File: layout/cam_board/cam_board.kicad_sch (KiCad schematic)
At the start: 73 parts, among them J1 Debug, J2 USB Connector, J3 BATT_CONNECTOR, J4 LCD conn, J5 Stick conn, Q1 BSS138, SW1 BOOT0, SW2 NRST, SW3 USER, SW4 ON/OFF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

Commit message: Update layout and schematic
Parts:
- added C6: 100nF, Capacitor_SMD:C_0402_1005Metric_Pad0.74x0.62mm_HandSolder, symbol Device:C
- added R23, R24: 10k, Resistor_SMD:R_0603_1608Metric_Pad0.98x0.95mm_HandSolder, symbol Device:R
- added U3: M24C16-RMN6TP, A_Custom:SOIC127P600X175-8N, symbol Custom:M24C16-RMN6TP
- SW1, SW2, SW4: footprint Button_Switch_SMD:SW_DIP_SPSTx01_Slide_9.78x4.72mm_W8.61mm_P2.54mm -> Button_Switch_SMD:SW_DIP_SPSTx01_Slide_6.7x4.1mm_W8.61mm_P2.54mm_LowProfile
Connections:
- net +3V3: now also C6.2, R23.2, R24.1, U3.8 (VCC)
- net GND: now also C6.1, U3.1 (E0), U3.2 (E1), U3.3 (E2), U3.4 (VSS)
- net EEPROM_NWC: now reaches U1.41 (PB5)
- net EEPROM_NWC: now also U3.7 (~{WC})
- net EEPROM_SCL: now reaches U1.42 (PB6)
- net EEPROM_SCL: now also R23.1, U3.6 (SCL)
- net EEPROM_SDA: now reaches U1.43 (PB7)
- net EEPROM_SDA: now also R24.2, U3.5 (SDA)
- no-connect marks 8 -> 5
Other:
- note added: "I2C-EEPROM"
- note removed: "SPI-Flash?"
- moved on the sheet: C10, C11, C12, C13, C18, C8, C9, R1, R2, R7, SW1, SW2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

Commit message: Update layout and schematic
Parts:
- added JP1: Battery Bypass, Jumper:SolderJumper-3_P1.3mm_Open_RoundedPad1.0x1.5mm_NumberLabels, symbol Jumper:SolderJumper_3_Open
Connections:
- net VIN: now also JP1.2 (C); no longer C21.2, U5.18 (IN), U5.19 (IN)
- net VOUT: now also JP1.1 (A)
- new net: C21.2, JP1.3 (B), U5.18 (IN), U5.19 (IN)
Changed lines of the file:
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@@
 	)
 	(junction
-		(at 220.98 33.02)
-		(diameter 0)
-		(color 0 0 0 0)
-	)
-	(junction
 		(at 137.16 35.56)
 		(diameter 0)
@@
 	)
 	(junction
+		(at 220.98 34.29)
+		(diameter 0)
+		(color 0 0 0 0)
+	)
+	(junction
 		(at 187.96 35.56)
 		(diameter 0)
@@
 	)
 	(junction
-		(at 224.79 29.21)
+		(at 43.18 185.42)
 		(diameter 0)
 		(color 0 0 0 0)
 	)
 	(junction
-		(at 43.18 185.42)
+		(at 190.5 81.28)
 		(diameter 0)
 		(color 0 0 0 0)
 	)
 	(junction
-		(at 190.5 81.28)
+		(at 228.6 29.21)
 		(diameter 0)
 		(color 0 0 0 0)
@@
 	)
 	(junction
+		(at 238.76 34.29)
+		(diameter 0)
+		(color 0 0 0 0)
+	)
+	(junction
 		(at 270.51 59.69)
 		(diameter 0)
@@
 	(wire
 		(pts
-			(xy 238.76 33.02) (xy 238.76 43.18)
+			(xy 238.76 33.02) (xy 238.76 34.29)
 		)
 		(stroke
@@
 	(wire
 		(pts
+			(xy 220.98 34.29) (xy 220.98 35.56)
+		)
+		(stroke
+			(width 0)
+			(type default)
+		)
+	)
+	(wire
+		(pts
 			(xy 43.18 184.15) (xy 43.18 185.42)
 		)
@@
 	(wire
 		(pts
-			(xy 224.79 29.21) (xy 237.49 29.21)
+			(xy 224.79 29.21) (xy 228.6 29.21)
 		)
 		(stroke
@@
 	(wire
 		(pts
-			(xy 220.98 33.02) (xy 220.98 35.56)
+			(xy 220.98 33.02) (xy 220.98 34.29)
 		)
 		(stroke
@@
 	(wire
 		(pts
-			(xy 220.98 33.02) (xy 224.79 33.02)
-		)
-		(stroke
-			(width 0)
-			(type default)
-		)
-	)
-	(wire
-		(pts
 			(xy 209.55 118.11) (xy 209.55 123.19)
 		)
@@
 	(wire
 		(pts
+			(xy 233.68 34.29) (xy 238.76 34.29)
+		)
+		(stroke
+			(width 0)
+			(type default)
+		)
+	)
+	(wire
+		(pts
 			(xy 158.75 45.72) (xy 158.75 44.45)
 		)
@@
 	(wire
 		(pts
+			(xy 238.76 34.29) (xy 238.76 43.18)
+		)
+		(stroke
+			(width 0)
+			(type default)
+		)
+	)
+	(wire
+		(pts
 			(xy 250.19 73.66) (xy 250.19 74.93)
 		)
@@
 	(wire
 		(pts
+			(xy 228.6 29.21) (xy 228.6 30.48)
+		)
+		(stroke
+			(width 0)
+			(type default)
+		)
+	)
+	(wire
+		(pts
 			(xy 43.18 173.99) (xy 43.18 175.26)
 		)
@@
 	(wire
 		(pts
+			(xy 228.6 29.21) (xy 237.49 29.21)
+		)
+		(stroke
+			(width 0)
+			(type default)
+		)
+	)
+	(wire
+		(pts
 			(xy 190.5 81.28) (xy 190.5 83.82)
 		)
@@
 	(wire
 		(pts
+			(xy 220.98 34.29) (xy 223.52 34.29)
+		)
+		(stroke
+			(width 0)
+			(type default)
+		)
+	)
+	(wire
+		(pts
 			(xy 151.13 173.99) (xy 153.67 173.99)
 		)
@@
 	(wire
 		(pts
-			(xy 224.79 29.21) (xy 224.79 33.02)
-		)
-		(stroke
-			(width 0)
-			(type default)
-		)
-	)
-	(wire
-		(pts
 			(xy 218.44 24.13) (xy 213.36 24.13)
 		)
@@
 					(unit 1)
 				)
+			)
+		)
+	)
+	(symbol
+		(lib_id "Jumper:SolderJumper_3_Open")
+		(at 228.6 34.29 180)
+		(unit 1)
+		(exclude_from_sim no)
+		(in_bom no)
+		(on_board yes)
+		(dnp no)
+		(property "Reference" "JP1"
+			(at 230.886 32.004 0)
+			(effects
+				(font
+					(size 1.27 1.27)
+				)
+			)
+		)
+		(property "Value" "Battery Bypass"
+			(at 229.362 36.83 0)
+			(effects
+				(font
+					(size 1.27 1.27)
+				)
+			)
+		)
+		(property "Footprint" "Jumper:SolderJumper-3_P1.3mm_Open_RoundedPad1.0x1.5mm_NumberLabels"
+			(at 228.6 34.29 0)
+			(effects
+				(font
+					(size 1.27 1.27)
+				)
+				(hide yes)
+			)
+		)
+		(property "Datasheet" "~"
+			(at 228.6 34.29 0)
+			(effects
+				(font
+					(size 1.27 1.27)
+				)
+				(hide yes)
+			)
+		)
+		(property "Description" "Solder Jumper, 3-pole, open"
+			(at 228.6 34.29 0)
+			(effects
+				(font
+					(size 1.27 1.27)
+				)
+				(hide yes)
+			)
+		)
+		(pin "3"
+		)
+		(pin "2"
+		)
+		(pin "1"
+		)
+		(instances
+			(project "cam_board"
+				(path "/eee23683-93c4-45fa-9c00-e358d0d25f58"
+					(reference "JP1")
+					(unit 1)
+				)

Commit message: Update layout and schematic
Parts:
- removed D2, D3: D_Schottky, Diode_SMD:D_0603_1608Metric_Pad1.05x0.95mm_HandSolder, symbol Device:D_Schottky
- removed J1: Debug, Connector_PinHeader_1.27mm:PinHeader_1x06_P1.27mm_Vertical, symbol Connector:Conn_01x06_Pin
- removed Q1: BSS138, Package_TO_SOT_SMD:SOT-23_Handsoldering, symbol Transistor_FET:BSS138
- added J1: Conn_01x04_Pin, Connector_PinHeader_1.27mm:PinHeader_1x04_P1.27mm_Vertical, symbol Connector:Conn_01x04_Pin
- C6: footprint Capacitor_SMD:C_0402_1005Metric_Pad0.74x0.62mm_HandSolder -> Capacitor_SMD:C_0603_1608Metric_Pad1.08x0.95mm_HandSolder
- R17: value 100k -> 100M
- R18: value 220k -> 220M
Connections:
- net USB+5V is gone; now on net VIN: C14.2, C15.2, D5.1 (K), U2.5 (VBUS)
- net GND: now also R18.1
- net NRST: now also J1.4 (Pin_4)
- net SWCLK: now also J1.1 (Pin_1)
- net SWDIO: now also J1.2 (Pin_2)
- net SWO: now also J1.3 (Pin_3)
- net BATTLVL_READ: no longer names the net of U1.25 (PB12)
- no-connect marks 5 -> 6
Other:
- note removed: "With the diode-or one can safely connect the LDO both with USB or Debug voltage ToDo: kann der SWD den ladestrom?"
- moved on the sheet: C23, R17, R18

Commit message: Update layout and schematic
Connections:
- net SWCLK: now also U1.37 (PA14); no longer U1.34 (PA13)
- net SWDIO: now also U1.34 (PA13); no longer U1.37 (PA14)
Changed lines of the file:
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@@
 		)
 	)
-	(global_label "SWDIO"
-		(shape input)
-		(at 156.21 95.25 0)
-		(fields_autoplaced yes)
-		(effects
-			(font
-				(size 1.27 1.27)
-			)
-			(justify left)
-		)
-		(property "Intersheetrefs" "${INTERSHEET_REFS}"
-			(at 165.0614 95.25 0)
-			(effects
-				(font
-					(size 1.27 1.27)
-				)
-				(justify left)
-				(hide yes)
-			)
-		)
-	)
 	(global_label "DC"
 		(shape input)
@@
 		)
 	)
+	(global_label "SWDIO"
+		(shape input)
+		(at 156.21 92.71 0)
+		(fields_autoplaced yes)
+		(effects
+			(font
+				(size 1.27 1.27)
+			)
+			(justify left)
+		)
+		(property "Intersheetrefs" "${INTERSHEET_REFS}"
+			(at 165.0614 92.71 0)
+			(effects
+				(font
+					(size 1.27 1.27)
+				)
+				(justify left)
+				(hide yes)
+			)
+		)
+	)
 	(global_label "D+"
 		(shape input)
@@
 		)
 	)
-	(global_label "SWCLK"
-		(shape input)
-		(at 156.21 92.71 0)
-		(fields_autoplaced yes)
-		(effects
-			(font
-				(size 1.27 1.27)
-			)
-			(justify left)
-		)
-		(property "Intersheetrefs" "${INTERSHEET_REFS}"
-			(at 165.4242 92.71 0)
-			(effects
-				(font
-					(size 1.27 1.27)
-				)
-				(justify left)
-				(hide yes)
-			)
-		)
-	)
 	(global_label "BATTCHARGE"
 		(shape input)
@@
 		)
 	)
+	(global_label "SWCLK"
+		(shape input)
+		(at 156.21 95.25 0)
+		(fields_autoplaced yes)
+		(effects
+			(font
+				(size 1.27 1.27)
+			)
+			(justify left)
+		)
+		(property "Intersheetrefs" "${INTERSHEET_REFS}"
+			(at 165.4242 95.25 0)
+			(effects
+				(font
+					(size 1.27 1.27)
+				)
+				(justify left)
+				(hide yes)
+			)
+		)
+	)
 	(global_label "BATTCHARGING"
 		(shape input)
@@
 	)
 	(symbol
+		(lib_name "+5V_3")
 		(lib_id "power:+5V")
 		(at 250.19 54.61 0)
@@
 	)
 	(symbol
+		(lib_name "+5V_2")
 		(lib_id "power:+5V")
 		(at 228.6 21.59 0)
@@
 	)
 	(symbol
+		(lib_name "+5V_1")
 		(lib_id "power:+5V")
 		(at 187.96 26.67 0)
@@
 	)
 	(symbol
+		(lib_name "SolderJumper_3_Open_1")
 		(lib_id "Jumper:SolderJumper_3_Open")
 		(at 228.6 34.29 180)

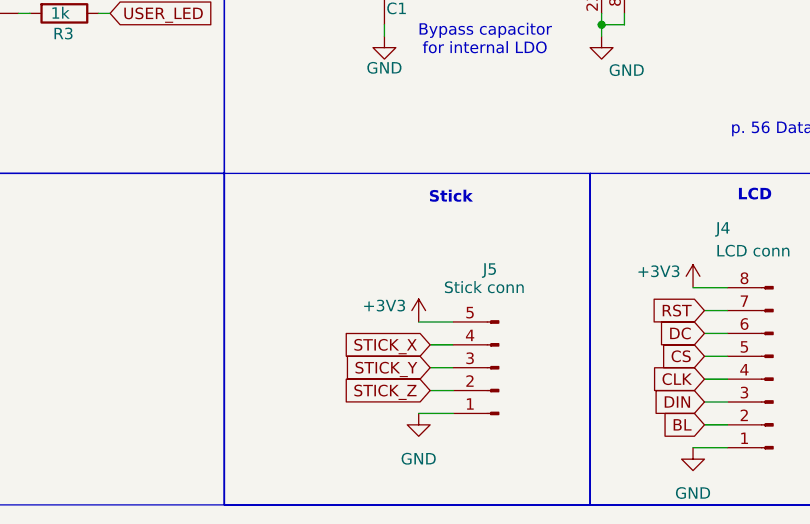
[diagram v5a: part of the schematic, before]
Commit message: Fix menu, add missing pull-up
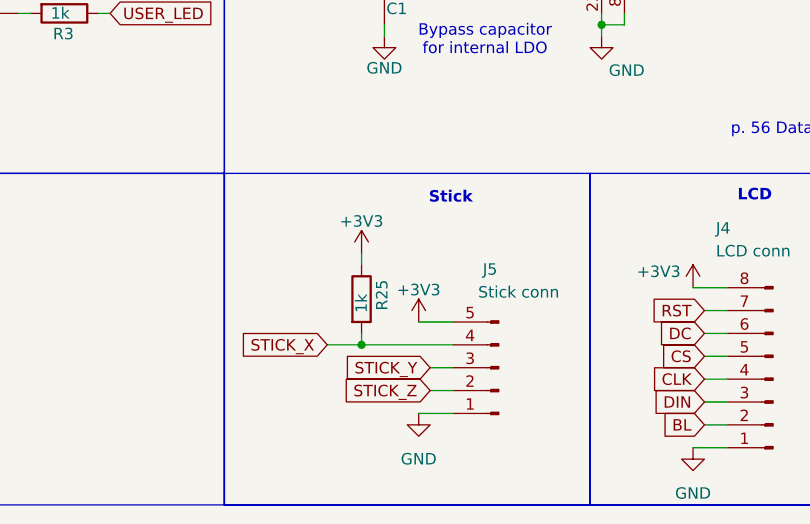
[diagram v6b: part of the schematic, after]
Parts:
- added R25: 1k, Resistor_SMD:R_0603_1608Metric_Pad0.98x0.95mm_HandSolder, symbol Device:R
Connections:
- net +3V3: now also R25.1
- net STICK_X: now also R25.2
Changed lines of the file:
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@@
 	)
 	(junction
+		(at 113.03 177.8)
+		(diameter 0)
+		(color 0 0 0 0)
+	)
+	(junction
 		(at 74.93 30.48)
 		(diameter 0)
@@
 	(wire
 		(pts
-			(xy 120.65 177.8) (xy 123.19 177.8)
+			(xy 109.22 177.8) (xy 113.03 177.8)
 		)
 		(stroke
@@
 	(wire
 		(pts
+			(xy 113.03 176.53) (xy 113.03 177.8)
+		)
+		(stroke
+			(width 0)
+			(type default)
+		)
+	)
+	(wire
+		(pts
 			(xy 220.98 33.02) (xy 220.98 34.29)
 		)
@@
 	(wire
 		(pts
+			(xy 113.03 167.64) (xy 113.03 168.91)
+		)
+		(stroke
+			(width 0)
+			(type default)
+		)
+	)
+	(wire
+		(pts
 			(xy 243.84 74.93) (xy 250.19 74.93)
 		)
@@
 	(wire
 		(pts
+			(xy 113.03 177.8) (xy 123.19 177.8)
+		)
+		(stroke
+			(width 0)
+			(type default)
+		)
+	)
+	(wire
+		(pts
 			(xy 275.59 125.73) (xy 275.59 124.46)
 		)
@@
 	(global_label "STICK_X"
 		(shape input)
-		(at 120.65 177.8 180)
+		(at 109.22 177.8 180)
 		(fields_autoplaced yes)
 		(effects
@@
 		)
 		(property "Intersheetrefs" "${INTERSHEET_REFS}"
-			(at 110.1658 177.8 0)
+			(at 98.7358 177.8 0)
 			(effects
 				(font
@@
 	)
 	(symbol
+		(lib_id "power:+3V3")
+		(at 113.03 167.64 0)
+		(unit 1)
+		(exclude_from_sim no)
+		(in_bom yes)
+		(on_board yes)
+		(dnp no)
+		(property "Reference" "#PWR02"
+			(at 113.03 171.45 0)
+			(effects
+				(font
+					(size 1.27 1.27)
+				)
+				(hide yes)
+			)
+		)
+		(property "Value" "+3V3"
+			(at 113.03 164.084 0)
+			(effects
+				(font
+					(size 1.27 1.27)
+				)
+			)
+		)
+		(property "Footprint" ""
+			(at 113.03 167.64 0)
+			(effects
+				(font
+					(size 1.27 1.27)
+				)
+				(hide yes)
+			)
+		)
+		(property "Datasheet" ""
+			(at 113.03 167.64 0)
+			(effects
+				(font
+					(size 1.27 1.27)
+				)
+				(hide yes)
+			)
+		)
+		(property "Description" "Power symbol creates a global label with name \"+3V3\""
+			(at 113.03 167.64 0)
+			(effects
+				(font
+					(size 1.27 1.27)
+				)
+				(hide yes)
+			)
+		)
+		(pin "1"
+		)
+		(instances
+			(project "cam_board"
+				(path "/eee23683-93c4-45fa-9c00-e358d0d25f58"
+					(reference "#PWR02")
+					(unit 1)
+				)
+			)
+		)
+	)
+	(symbol
 		(lib_id "power:GND")
 		(at 259.08 125.73 0)
@@
 		)
 		(property "Value" "Stick conn"
-			(at 122.174 171.45 0)
+			(at 125.984 171.958 0)
 			(effects
 				(font
@@
 	)
 	(symbol
+		(lib_id "Device:R")
+		(at 113.03 172.72 0)
+		(unit 1)
+		(exclude_from_sim no)
+		(in_bom yes)
+		(on_board yes)
+		(dnp no)
+		(property "Reference" "R25"
+			(at 115.316 173.99 90)
+			(effects
+				(font
+					(size 1.27 1.27)
+				)
+				(justify left)
+			)
+		)
+		(property "Value" "1k"
+			(at 113.03 174.244 90)
+			(effects
+				(font
+					(size 1.27 1.27)
+				)
+				(justify left)
+			)
+		)
+		(property "Footprint" "Resistor_SMD:R_0603_1608Metric_Pad0.98x0.95mm_HandSolder"
+			(at 111.252 172.72 90)
+			(effects
+				(font
+					(size 1.27 1.27)
+				)
+				(hide yes)
+			)
+		)
+		(property "Datasheet" "~"
+			(at 113.03 172.72 0)
+			(effects
+				(font
+					(size 1.27 1.27)
+				)
+				(hide yes)
+			)
+		)
+		(property "Description" "Resistor"
+			(at 113.03 172.72 0)
+			(effects
+				(font
+					(size 1.27 1.27)
+				)
+				(hide yes)
+			)
+		)
+		(pin "2"
+		)
+		(pin "1"
+		)
+		(instances
+			(project "cam_board"
+				(path "/eee23683-93c4-45fa-9c00-e358d0d25f58"
+					(reference "R25")
+					(unit 1)
+				)
+			)
+		)
+	)
+	(symbol
 		(lib_id "Device:C")
 		(at 109.22 74.93 180)
@@
 		)
 		(property "Value" "+3V3"
-			(at 115.57 173.482 0)
+			(at 119.38 171.704 0)
 			(effects
 				(font

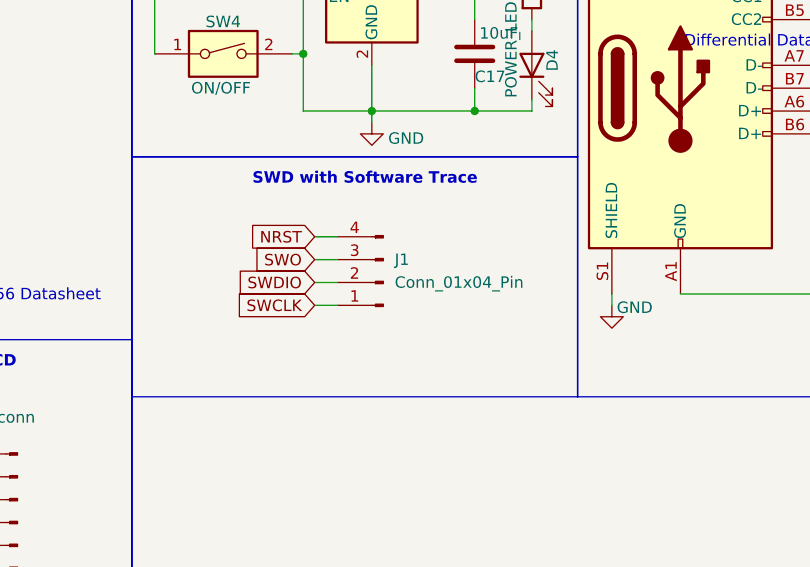
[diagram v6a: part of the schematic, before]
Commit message: Prepare USB and fix missing GND line in layout
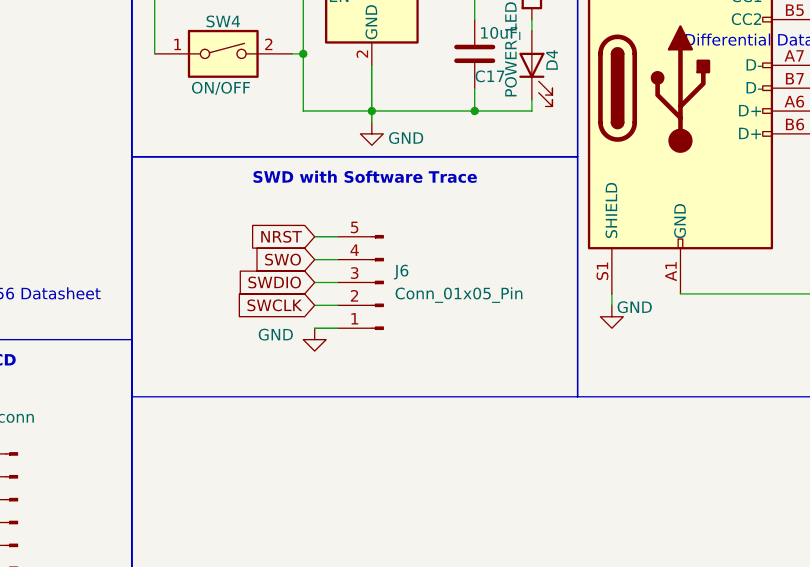
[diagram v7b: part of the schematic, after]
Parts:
- removed J1: Conn_01x04_Pin, Connector_PinHeader_1.27mm:PinHeader_1x04_P1.27mm_Vertical, symbol Connector:Conn_01x04_Pin
- added J6: Conn_01x05_Pin, Connector_PinHeader_1.27mm:PinHeader_1x05_P1.27mm_Vertical, symbol Connector:Conn_01x05_Pin
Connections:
- net GND: now also J6.1 (Pin_1)
- net NRST: now also J6.5 (Pin_5)
- net SWCLK: now also J6.2 (Pin_2)
- net SWDIO: now also J6.3 (Pin_3)
- net SWO: now also J6.4 (Pin_4)
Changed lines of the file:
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@@
 	(wire
 		(pts
+			(xy 191.77 157.48) (xy 194.31 157.48)
+		)
+		(stroke
+			(width 0)
+			(type default)
+		)
+	)
+	(wire
+		(pts
 			(xy 109.22 80.01) (xy 100.33 80.01)
 		)
@@
 	)
 	(symbol
-		(lib_id "Connector:Conn_01x04_Pin")
-		(at 199.39 152.4 180)
-		(unit 1)
-		(exclude_from_sim no)
-		(in_bom yes)
-		(on_board yes)
-		(dnp no)
-		(fields_autoplaced yes)
-		(property "Reference" "J1"
-			(at 200.66 149.8599 0)
-			(effects
-				(font
-					(size 1.27 1.27)
-				)
-				(justify right)
-			)
-		)
-		(property "Value" "Conn_01x04_Pin"
-			(at 200.66 152.3999 0)
-			(effects
-				(font
-					(size 1.27 1.27)
-				)
-				(justify right)
-			)
-		)
-		(property "Footprint" "Connector_PinHeader_1.27mm:PinHeader_1x04_P1.27mm_Vertical"
-			(at 199.39 152.4 0)
-			(effects
-				(font
-					(size 1.27 1.27)
-				)
-				(hide yes)
-			)
-		)
-		(property "Datasheet" "~"
-			(at 199.39 152.4 0)
-			(effects
-				(font
-					(size 1.27 1.27)
-				)
-				(hide yes)
-			)
-		)
-		(property "Description" "Generic connector, single row, 01x04, script generated"
-			(at 199.39 152.4 0)
-			(effects
-				(font
-					(size 1.27 1.27)
-				)
-				(hide yes)
-			)
-		)
-		(pin "4"
-		)
-		(pin "2"
-		)
-		(pin "1"
-		)
-		(pin "3"
-		)
-		(instances
-			(project ""
-				(path "/eee23683-93c4-45fa-9c00-e358d0d25f58"
-					(reference "J1")
-					(unit 1)
-				)
-			)
-		)
-	)
-	(symbol
 		(lib_id "Switch:SW_DIP_x01")
 		(at 181.61 127 0)
@@
 	)
 	(symbol
+		(lib_id "power:GND")
+		(at 191.77 157.48 0)
+		(unit 1)
+		(exclude_from_sim no)
+		(in_bom yes)
+		(on_board yes)
+		(dnp no)
+		(property "Reference" "#PWR09"
+			(at 191.77 163.83 0)
+			(effects
+				(font
+					(size 1.27 1.27)
+				)
+				(hide yes)
+			)
+		)
+		(property "Value" "GND"
+			(at 187.452 158.242 0)
+			(effects
+				(font
+					(size 1.27 1.27)
+				)
+			)
+		)
+		(property "Footprint" ""
+			(at 191.77 157.48 0)
+			(effects
+				(font
+					(size 1.27 1.27)
+				)
+				(hide yes)
+			)
+		)
+		(property "Datasheet" ""
+			(at 191.77 157.48 0)
+			(effects
+				(font
+					(size 1.27 1.27)
+				)
+				(hide yes)
+			)
+		)
+		(property "Description" "Power symbol creates a global label with name \"GND\" , ground"
+			(at 191.77 157.48 0)
+			(effects
+				(font
+					(size 1.27 1.27)
+				)
+				(hide yes)
+			)
+		)
+		(pin "1"
+		)
+		(instances
+			(project "cam_board"
+				(path "/eee23683-93c4-45fa-9c00-e358d0d25f58"
+					(reference "#PWR09")
+					(unit 1)
+				)
+			)
+		)
+	)
+	(symbol
 		(lib_id "Device:C")
 		(at 41.91 142.24 180)
@@
 					(unit 1)
 				)
+			)
+		)
+	)
+	(symbol
+		(lib_id "Connector:Conn_01x05_Pin")
+		(at 199.39 152.4 180)
+		(unit 1)
+		(exclude_from_sim no)
+		(in_bom yes)
+		(on_board yes)
+		(dnp no)
+		(fields_autoplaced yes)
+		(property "Reference" "J6"
+			(at 200.66 151.1299 0)
+			(effects
+				(font
+					(size 1.27 1.27)
+				)
+				(justify right)
+			)
+		)
+		(property "Value" "Conn_01x05_Pin"
+			(at 200.66 153.6699 0)
+			(effects
+				(font
+					(size 1.27 1.27)
+				)
+				(justify right)
+			)
+		)
+		(property "Footprint" "Connector_PinHeader_1.27mm:PinHeader_1x05_P1.27mm_Vertical"
+			(at 199.39 152.4 0)
+			(effects
+				(font
+					(size 1.27 1.27)
+				)
+				(hide yes)
+			)
+		)
+		(property "Datasheet" "~"
+			(at 199.39 152.4 0)
+			(effects
+				(font
+					(size 1.27 1.27)
+				)
+				(hide yes)
+			)
+		)
+		(property "Description" "Generic connector, single row, 01x05, script generated"
+			(at 199.39 152.4 0)
+			(effects
+				(font
+					(size 1.27 1.27)
+				)
+				(hide yes)
+			)
+		)
+		(pin "1"
+		)
+		(pin "2"
+		)
+		(pin "3"
+		)
+		(pin "5"
+		)
+		(pin "4"
+		)
+		(instances
+			(project ""
+				(path "/eee23683-93c4-45fa-9c00-e358d0d25f58"
+					(reference "J6")
+					(unit 1)
+				)

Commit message: Update board and layout
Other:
- note removed: "ToDo: Datenblatt checken, Widerstände checken. Ausgangsspannung mit LDO prüfen (wie viel droput). Thermal management beachten, CE check"
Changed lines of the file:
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@@
-		)
-	)
-	(text "ToDo: Datenblatt checken, Widerstände checken. \nAusgangsspannung mit LDO prüfen (wie viel droput).\nThermal management beachten, CE check"
-		(exclude_from_sim no)
-		(at 319.278 64.516 0)
-		(effects
-			(font
-				(size 1.27 1.27)
-			)
 		)
 	)
